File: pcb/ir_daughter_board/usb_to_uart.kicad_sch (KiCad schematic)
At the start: 15 parts, among them U1 MCP2200T-I/SS, Y1 Crystal

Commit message: minor editorial changes
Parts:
- Y1: value Crystal -> 12,0000-HC49-SMD
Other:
- moved on the sheet: C5, C6, D2, D3, D4, D5, R1, R2, R4, R5, R6, R7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

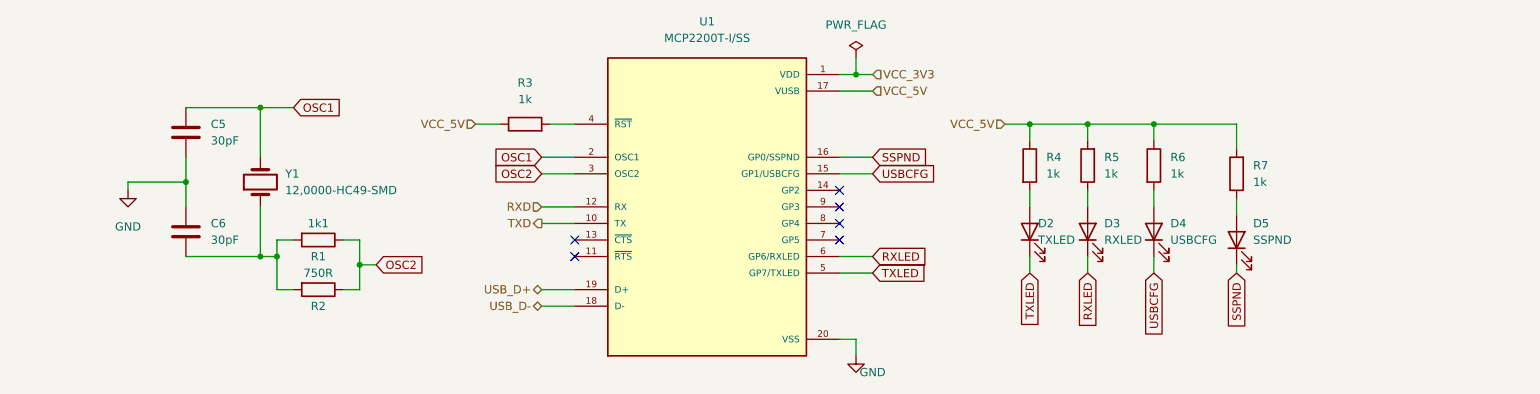
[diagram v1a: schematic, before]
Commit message: refined circuit with reddit comments
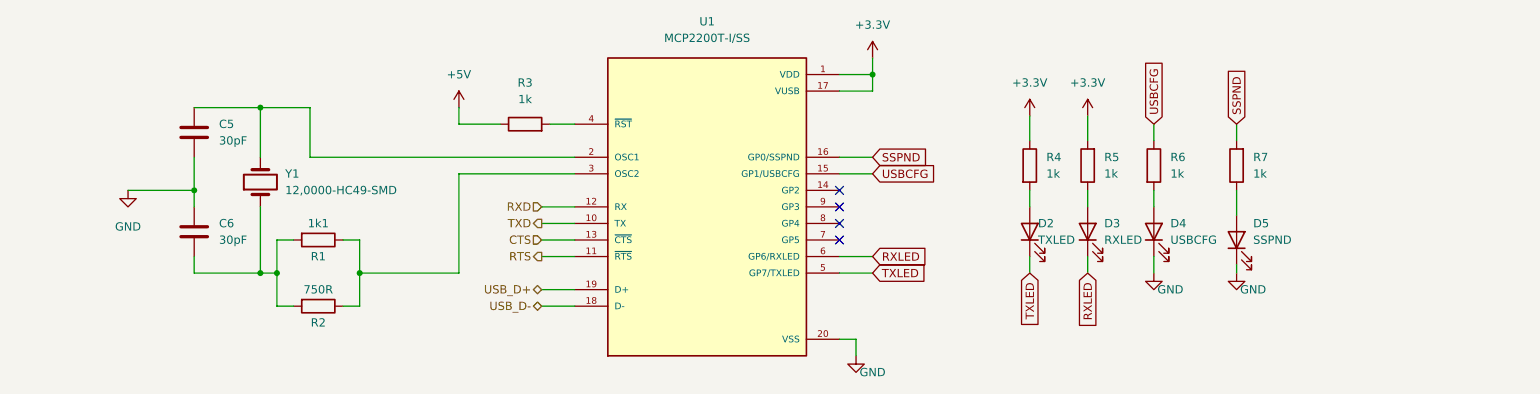
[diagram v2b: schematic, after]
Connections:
- net GND: now also D4.1 (K), D5.1 (K)
- net SSPND: now also R7.2; no longer D5.1 (K)
- net USBCFG: now also R6.1; no longer D4.1 (K)
- net RTS: now reaches U1.11 (~{RTS})
- net CTS: now reaches U1.13 (~{CTS})
- net OSC1: no longer names the net of C5.1, U1.2 (OSC1), Y1.2
- net OSC2: no longer names the net of R1.1, R2.1, U1.3 (OSC2)
- net VCC_3V3 renamed +3V3
- net +3V3: now also R4.1, R5.2, U1.17 (VUSB)
- removed net VCC_5V: R3.1, R4.1, R5.2, R6.1, R7.2, U1.17 (VUSB)
- new net +5V: R3.1
- no-connect marks 6 -> 4
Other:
- moved on the sheet: C5, C6, R2, R7

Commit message: change MCP2200 footprint to standard footprint
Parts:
- U1: footprint MCP2200T-I_SS:SOP65P780X200-20N -> Package_SO:SSOP-20_5.3x7.2mm_P0.65mm
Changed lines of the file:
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@@
     (property "Reference" "U1" (id 0) (at 132.08 24.892 0))
     (property "Value" "MCP2200T-I/SS" (id 1) (at 132.08 27.432 0))
-    (property "Footprint" "MCP2200T-I_SS:SOP65P780X200-20N" (id 2) (at 132.08 53.34 0)
+    (property "Footprint" "Package_SO:SSOP-20_5.3x7.2mm_P0.65mm" (id 2) (at 132.08 53.34 0)
       (effects (font (size 1.27 1.27)) (justify left bottom) hide)
     )

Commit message: minor update in PCB
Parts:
- added C3: 100nF, Capacitor_SMD:C_0603_1608Metric, symbol Device:C
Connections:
- net +3V3: now also C3.1
- net GND: now also C3.2
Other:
- moved on the sheet: D2, D3, D4, D5, R4, R5, R6, R7

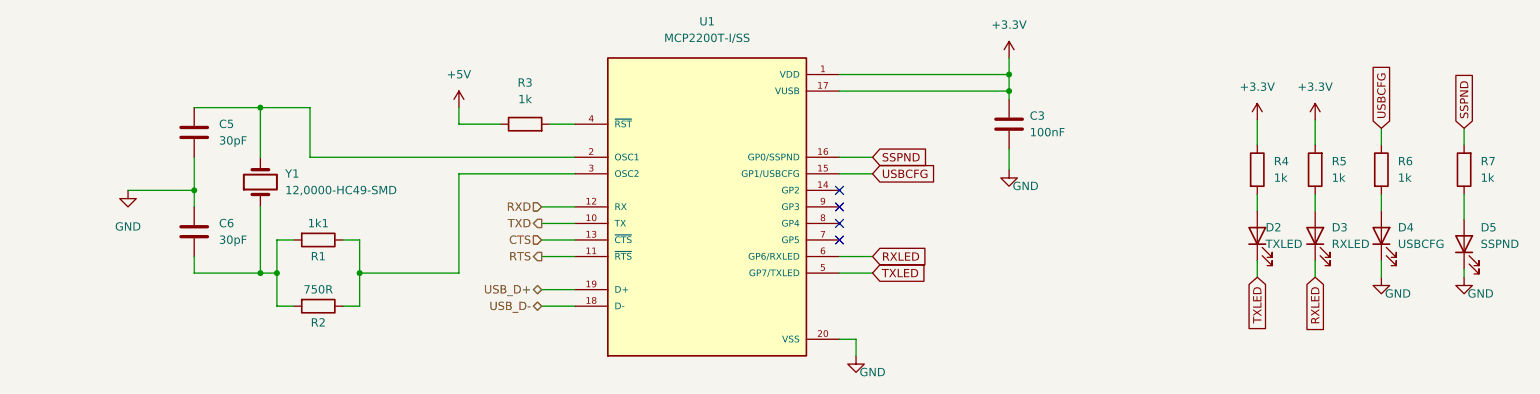
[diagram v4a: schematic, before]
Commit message: minor updateds in references and values
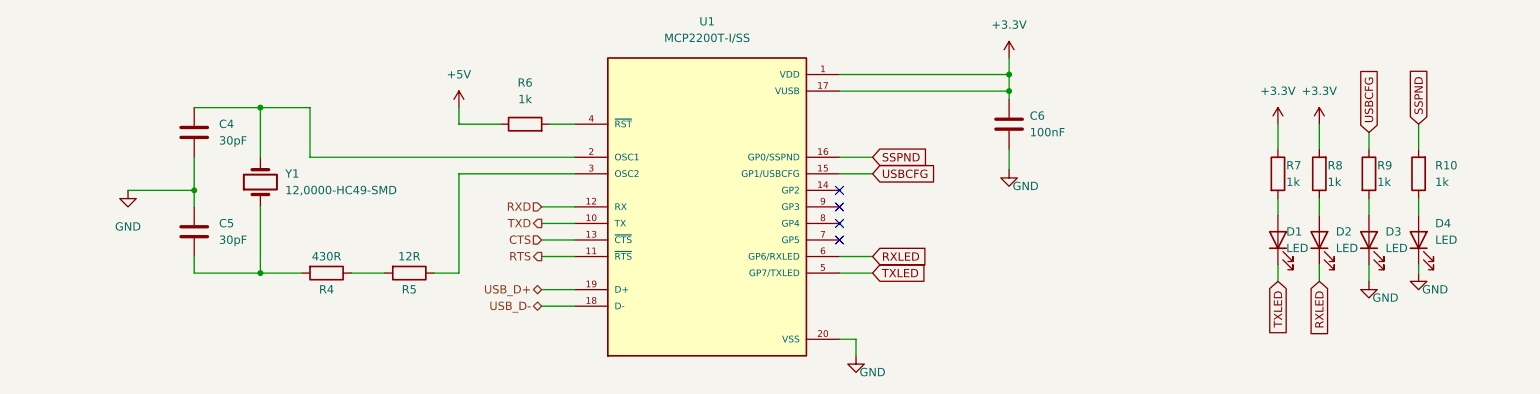
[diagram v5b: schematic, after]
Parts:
- D1: renamed from D2; value TXLED -> LED
- D2: renamed from D3; value RXLED -> LED
- D3: renamed from D4; value USBCFG -> LED
- D4: renamed from D5; value SSPND -> LED
- R4: renamed from R1; value 1k1 -> 430R
- R5: renamed from R2; value 750R -> 12R
- renumbered C5 to C4, C6 to C5, C3 to C6, R7 to R10, R3 to R6, R4 to R7, R5 to R8, R6 to R9
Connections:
- net at R5.1, U1.3 (OSC2): no longer R4.1
- net at C5.2, R4.2, Y1.1: no longer R5.2
- new net: R4.1, R5.2
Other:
- moved on the sheet: D1, D2, D3, D4, R10, R4, R5, R7, R8, R9
